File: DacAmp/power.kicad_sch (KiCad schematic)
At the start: 25 parts, among them U10 TLV70237_SOT23-5, U11 TLV61046ADB, U12 NE5532, U13 LM2941LD_NOPB

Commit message: get ready for layout
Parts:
- removed R32, R33: 1R, Resistor_SMD:R_0603_1608Metric_Pad0.98x0.95mm_HandSolder, symbol Device:R_US
- removed TP3: TestPoint, TestPoint:TestPoint_Pad_D1.5mm, symbol Connector:TestPoint
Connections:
- net 7V5_BUF1 renamed 7V5_R
- net 7V5_BUF2 renamed 7V5_L

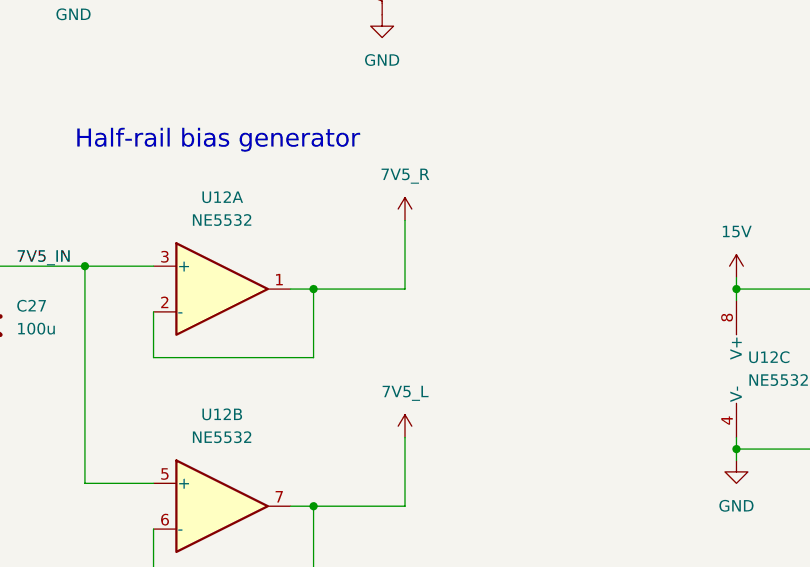
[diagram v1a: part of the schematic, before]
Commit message: add outputs for release 2
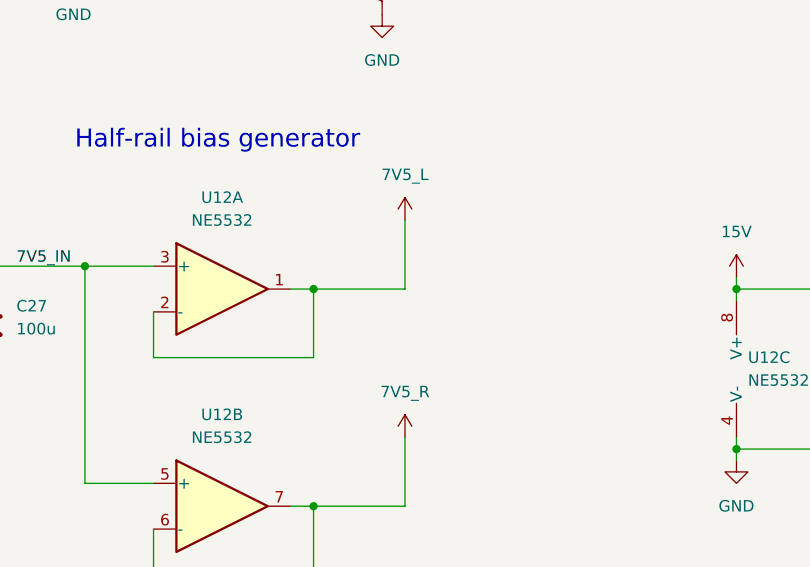
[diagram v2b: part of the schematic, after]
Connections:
- net 7V5_L: now also U12.1, U12.2 (-); no longer U12.6 (-), U12.7
- net 7V5_R: now also U12.6 (-), U12.7; no longer U12.1, U12.2 (-)
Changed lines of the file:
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@@
 	(symbol
 		(lib_id "power:VCC")
-		(at 114.3 151.13 0)
+		(at 114.3 127 0)
 		(unit 1)
 		(exclude_from_sim no)
@@
 		(fields_autoplaced yes)
 		(property "Reference" "#PWR081"
-			(at 114.3 154.94 0)
+			(at 114.3 130.81 0)
 			(effects
 				(font
@@
 		)
 		(property "Value" "7V5_L"
-			(at 114.3 146.05 0)
+			(at 114.3 121.92 0)
 			(effects
 				(font
@@
 		)
 		(property "Footprint" ""
-			(at 114.3 151.13 0)
+			(at 114.3 127 0)
 			(effects
 				(font
@@
 		)
 		(property "Datasheet" ""
-			(at 114.3 151.13 0)
+			(at 114.3 127 0)
 			(effects
 				(font
@@
 		)
 		(property "Description" "Power symbol creates a global label with name \"VCC\""
-			(at 114.3 151.13 0)
+			(at 114.3 127 0)
 			(effects
 				(font
@@
 	(symbol
 		(lib_id "power:VCC")
-		(at 114.3 127 0)
+		(at 114.3 151.13 0)
 		(unit 1)
 		(exclude_from_sim no)
@@
 		(fields_autoplaced yes)
 		(property "Reference" "#PWR044"
-			(at 114.3 130.81 0)
+			(at 114.3 154.94 0)
 			(effects
 				(font
@@
 		)
 		(property "Value" "7V5_R"
-			(at 114.3 121.92 0)
+			(at 114.3 146.05 0)
 			(effects
 				(font
@@
 		)
 		(property "Footprint" ""
-			(at 114.3 127 0)
+			(at 114.3 151.13 0)
 			(effects
 				(font
@@
 		)
 		(property "Datasheet" ""
-			(at 114.3 127 0)
+			(at 114.3 151.13 0)
 			(effects
 				(font
@@
 		)
 		(property "Description" "Power symbol creates a global label with name \"VCC\""
-			(at 114.3 127 0)
-			(effects
-				(font
+			(at 114.3 151.13 0)
+			(effects
+				(font
